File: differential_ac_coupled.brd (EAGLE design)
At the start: 66 x 57.7 mm, 27 parts, among them U1 AD8421

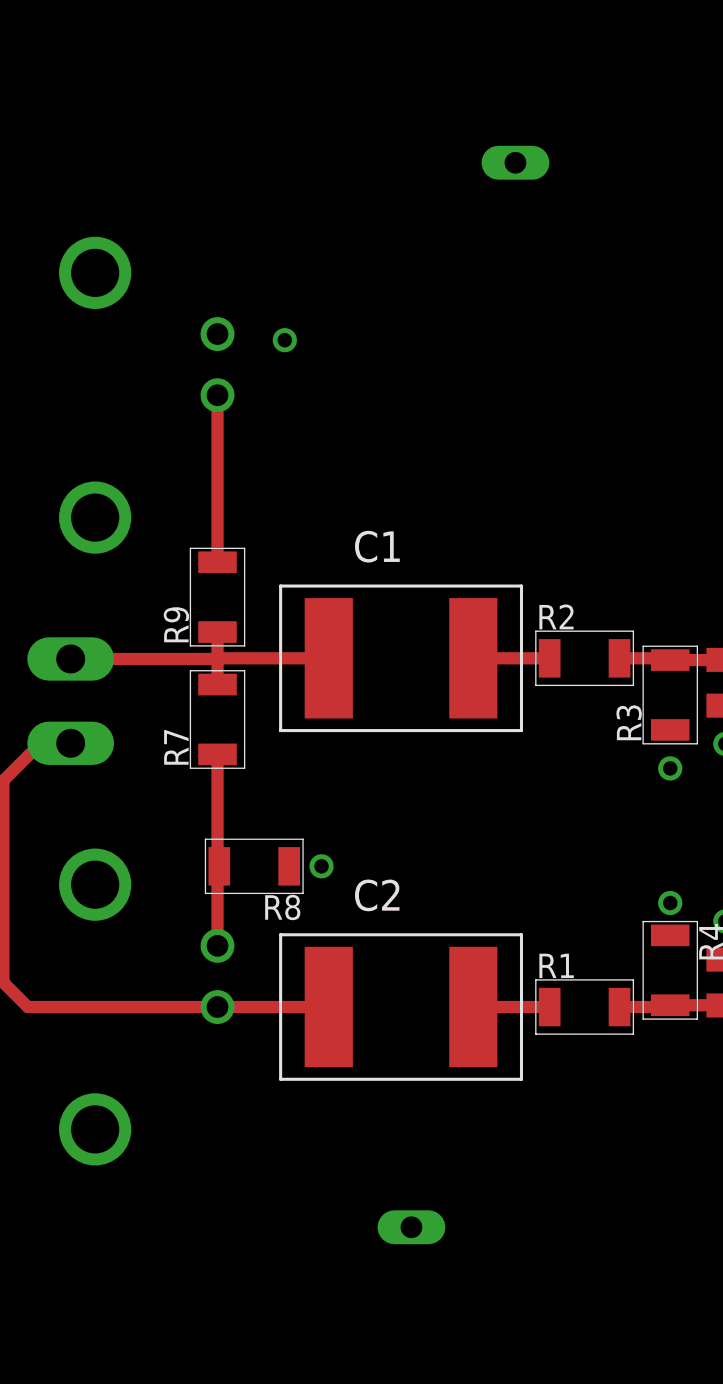
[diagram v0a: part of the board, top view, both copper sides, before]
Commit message: fixed bottom layer isolation; gnd via names
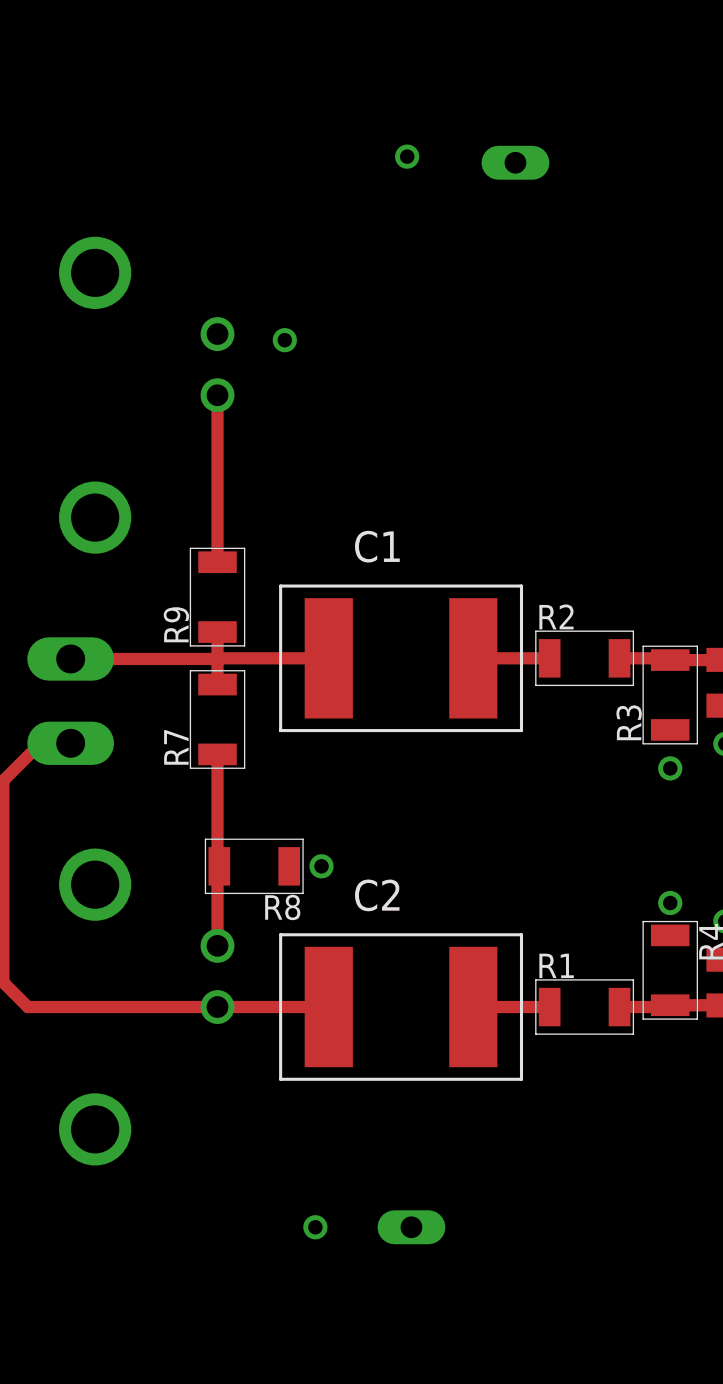
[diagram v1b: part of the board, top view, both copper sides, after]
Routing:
- net GND: vias 11 -> 14
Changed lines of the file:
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@@
 <wire x1="49.53" y1="11.176" x2="47.994" y2="11.176" width="0.508" layer="1"/>
 <wire x1="47.994" y1="17.78" x2="49.276" y2="17.78" width="0.508" layer="1"/>
-<polygon width="0.4064" layer="16">
+<polygon width="0.4064" layer="16" isolate="1.27">
 <vertex x="0" y="50.038"/>
 <vertex x="66.04" y="50.038"/>
@@
 <via x="49.784" y="30.48" extent="1-16" drill="0.6"/>
 <via x="17.018" y="13.462" extent="1-16" drill="0.6"/>
+<via x="15.494" y="35.306" extent="1-16" drill="0.6"/>
+<via x="20.574" y="42.926" extent="1-16" drill="0.6"/>
+<via x="16.764" y="-1.524" extent="1-16" drill="0.6"/>
 </signal>
 <signal name="N$7">
@@
 <wire x1="12.7" y1="13.388" x2="12.774" y2="13.462" width="0.508" layer="1"/>
 </signal>
-<signal name="N$21">
-<via x="15.494" y="35.306" extent="1-16" drill="0.6"/>
-</signal>
 </signals>
